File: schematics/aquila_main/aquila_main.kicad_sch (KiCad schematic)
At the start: 125 parts

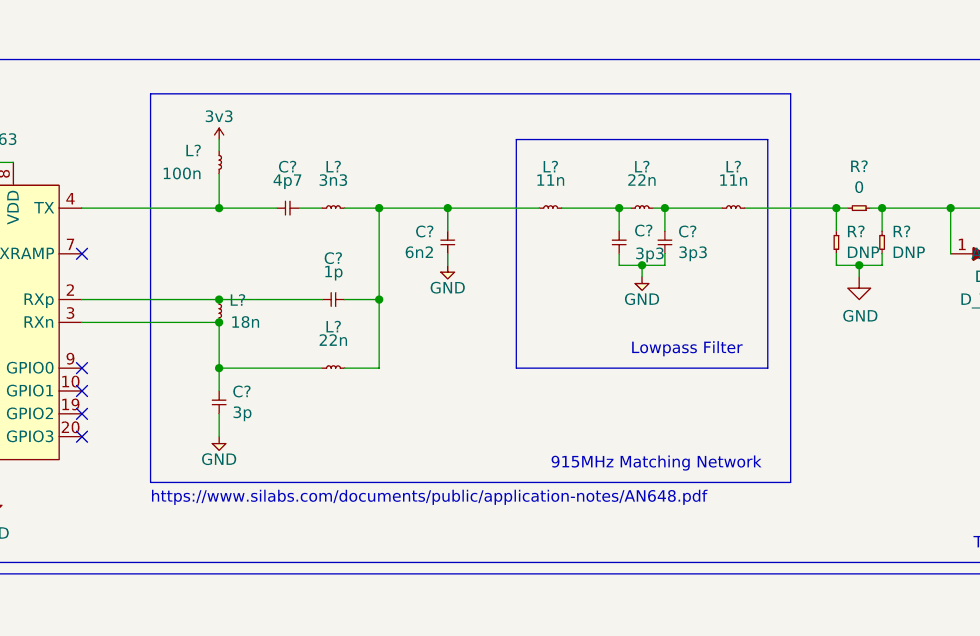
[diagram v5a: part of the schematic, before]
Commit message: changed to 868MHz matching on radio
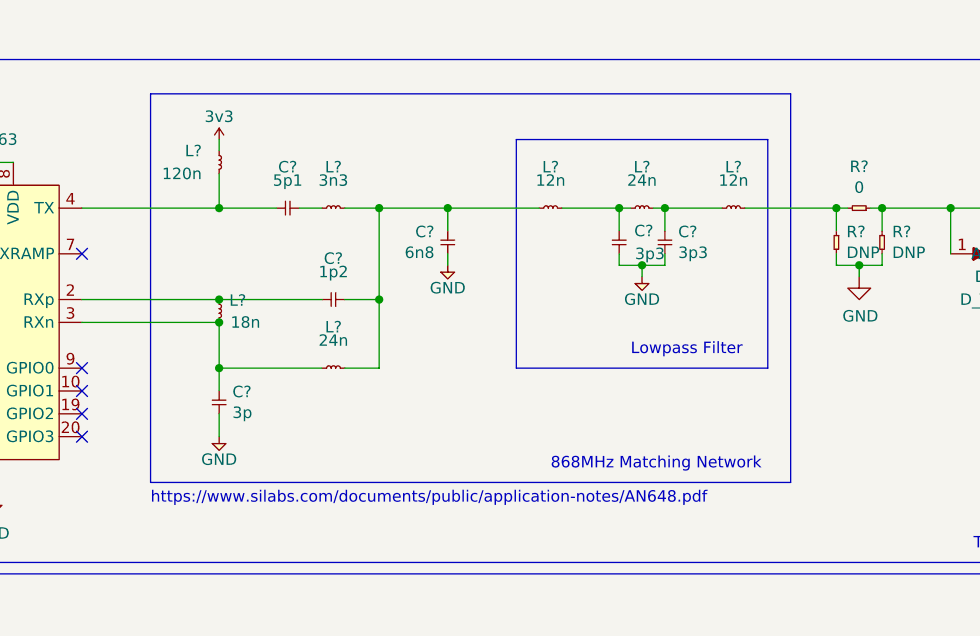
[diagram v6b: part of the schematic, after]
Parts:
- C?: value 1p -> 1p2
- C?: value 6n2 -> 6n8
- C?: value 4p7 -> 5p1
- L? (x2): value 11n -> 12n
- L?: value 100n -> 120n
- L? (x2): value 22n -> 24n
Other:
- note added: "868MHz Matching Network"
- note removed: "915MHz Matching Network"
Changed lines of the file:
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@@
     (effects (font (size 1.27 1.27)) (justify left bottom))
   )
-  (text "915MHz Matching Network" (at 148.59 191.77 0)
+  (text "868MHz Matching Network" (at 148.59 191.77 0)
     (effects (font (size 1.27 1.27)) (justify left bottom))
   )
@@
       (effects (font (size 1.27 1.27)) (justify bottom))
     )
-    (property "Value" "11n" (id 1) (at 148.59 158.75 0)
+    (property "Value" "12n" (id 1) (at 148.59 158.75 0)
       (effects (font (size 1.27 1.27)) (justify top))
     )
@@
       (effects (font (size 1.27 1.27)) (justify bottom))
     )
-    (property "Value" "1p" (id 1) (at 124.46 168.91 0)
+    (property "Value" "1p2" (id 1) (at 124.46 168.91 0)
       (effects (font (size 1.27 1.27)) (justify top))
     )
@@
       (effects (font (size 1.27 1.27)) (justify bottom))
     )
-    (property "Value" "11n" (id 1) (at 168.91 158.75 0)
+    (property "Value" "12n" (id 1) (at 168.91 158.75 0)
       (effects (font (size 1.27 1.27)) (justify top))
     )
@@
       (effects (font (size 1.27 1.27)) (justify left))
     )
-    (property "Value" "6n2" (id 1) (at 135.6868 167.513 90)
+    (property "Value" "6n8" (id 1) (at 135.6868 167.513 90)
       (effects (font (size 1.27 1.27)) (justify left))
     )
@@
       (effects (font (size 1.27 1.27)) (justify left))
     )
-    (property "Value" "100n" (id 1) (at 105.41 158.75 90)
+    (property "Value" "120n" (id 1) (at 105.41 158.75 90)
       (effects (font (size 1.27 1.27)) (justify left))
     )
@@
       (effects (font (size 1.27 1.27)) (justify bottom))
     )
-    (property "Value" "22n" (id 1) (at 124.46 176.53 0)
+    (property "Value" "24n" (id 1) (at 124.46 176.53 0)
       (effects (font (size 1.27 1.27)) (justify top))
     )
@@
       (effects (font (size 1.27 1.27)) (justify bottom))
     )
-    (property "Value" "22n" (id 1) (at 158.75 158.75 0)
+    (property "Value" "24n" (id 1) (at 158.75 158.75 0)
       (effects (font (size 1.27 1.27)) (justify top))
     )
@@
       (effects (font (size 1.27 1.27)) (justify bottom))
     )
-    (property "Value" "4p7" (id 1) (at 119.38 158.75 0)
+    (property "Value" "5p1" (id 1) (at 119.38 158.75 0)
       (effects (font (size 1.27 1.27)) (justify top))
     )
@@
     )
     (path "/2507031b-f5f8-4904-8f00-05c1469bcb72"
-      (reference "C?") (unit 1) (value "1p") (footprint "Strix:C_0402")
+      (reference "C?") (unit 1) (value "1p2") (footprint "Strix:C_0402")
     )
     (path "/27d5dca1-8f4b-4ac0-a3bf-f07d7733003c"
@@
     )
     (path "/689141ce-3cb4-4f7d-80d2-c503f350478d"
-      (reference "C?") (unit 1) (value "6n2") (footprint "Strix:C_0402")
+      (reference "C?") (unit 1) (value "6n8") (footprint "Strix:C_0402")
     )
     (path "/6e3a9897-4767-45ac-8e89-755b689b7b7b"
@@
     )
     (path "/b06b7fb7-53f6-4d89-b46b-9418e53b1ff3"
-      (reference "C?") (unit 1) (value "4p7") (footprint "Strix:C_0402")
+      (reference "C?") (unit 1) (value "5p1") (footprint "Strix:C_0402")
     )
     (path "/c80e54df-b29e-4bec-83f1-f7d3fca646ef"
@@
     )
     (path "/1288b0d7-80e7-4aa8-ba26-28318595760b"
-      (reference "L?") (unit 1) (value "11n") (footprint "Strix:L_0402")
+      (reference "L?") (unit 1) (value "12n") (footprint "Strix:L_0402")
     )
     (path "/2bcdfdc0-13c6-4c2e-9736-75366b3d43f9"
-      (reference "L?") (unit 1) (value "11n") (footprint "Strix:L_0402")
+      (reference "L?") (unit 1) (value "12n") (footprint "Strix:L_0402")
     )
     (path "/479753ae-6b30-4476-9bcb-23c9de27d17f"
@@
     )
     (path "/79bfbd2f-d120-4bb9-b75e-4a2b67982552"
-      (reference "L?") (unit 1) (value "100n") (footprint "Strix:L_0402")
+      (reference "L?") (unit 1) (value "120n") (footprint "Strix:L_0402")
     )
     (path "/7b0286f7-fbd0-424c-b380-5667a0d39bc5"
@@
     )
     (path "/89ed38eb-1140-4ef1-a212-5194d0297225"
-      (reference "L?") (unit 1) (value "22n") (footprint "Strix:L_0402")
+      (reference "L?") (unit 1) (value "24n") (footprint "Strix:L_0402")
     )
     (path "/af4782b6-37a5-400f-8446-daf53b8807d6"
-      (reference "L?") (unit 1) (value "22n") (footprint "Strix:L_0402")
+      (reference "L?") (unit 1) (value "24n") (footprint "Strix:L_0402")
     )
     (path "/de56e1d2-438f-4de1-963e-76768a4e6948"

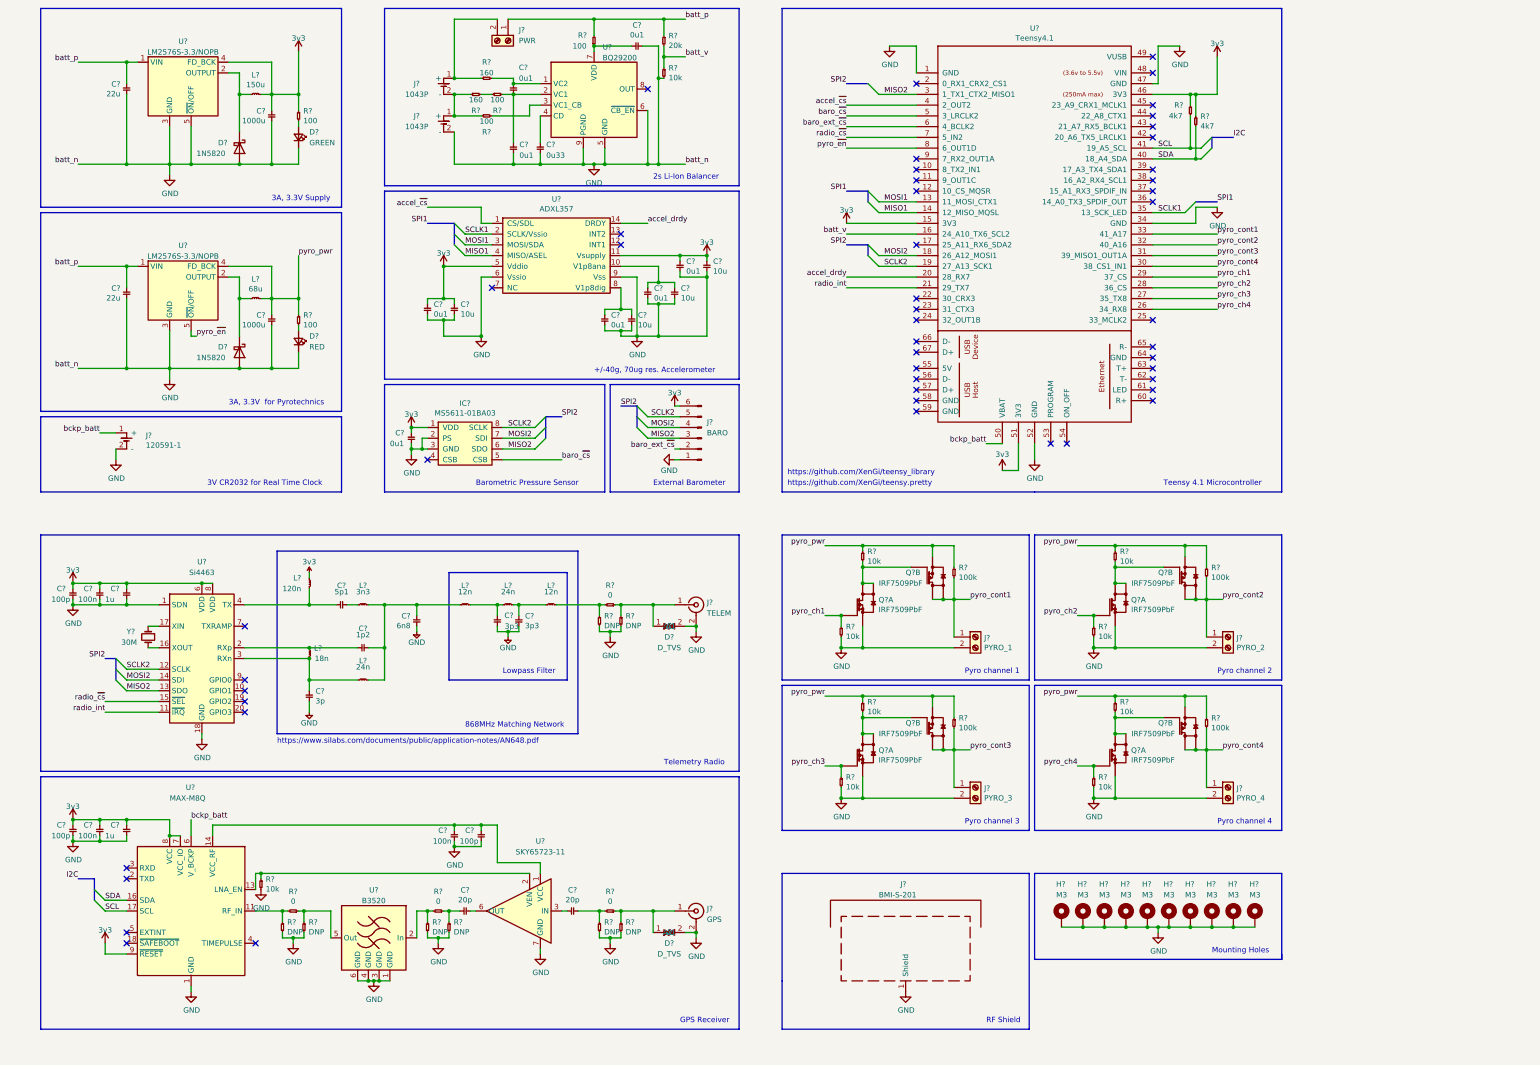
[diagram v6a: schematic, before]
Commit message: added pyro safety switch
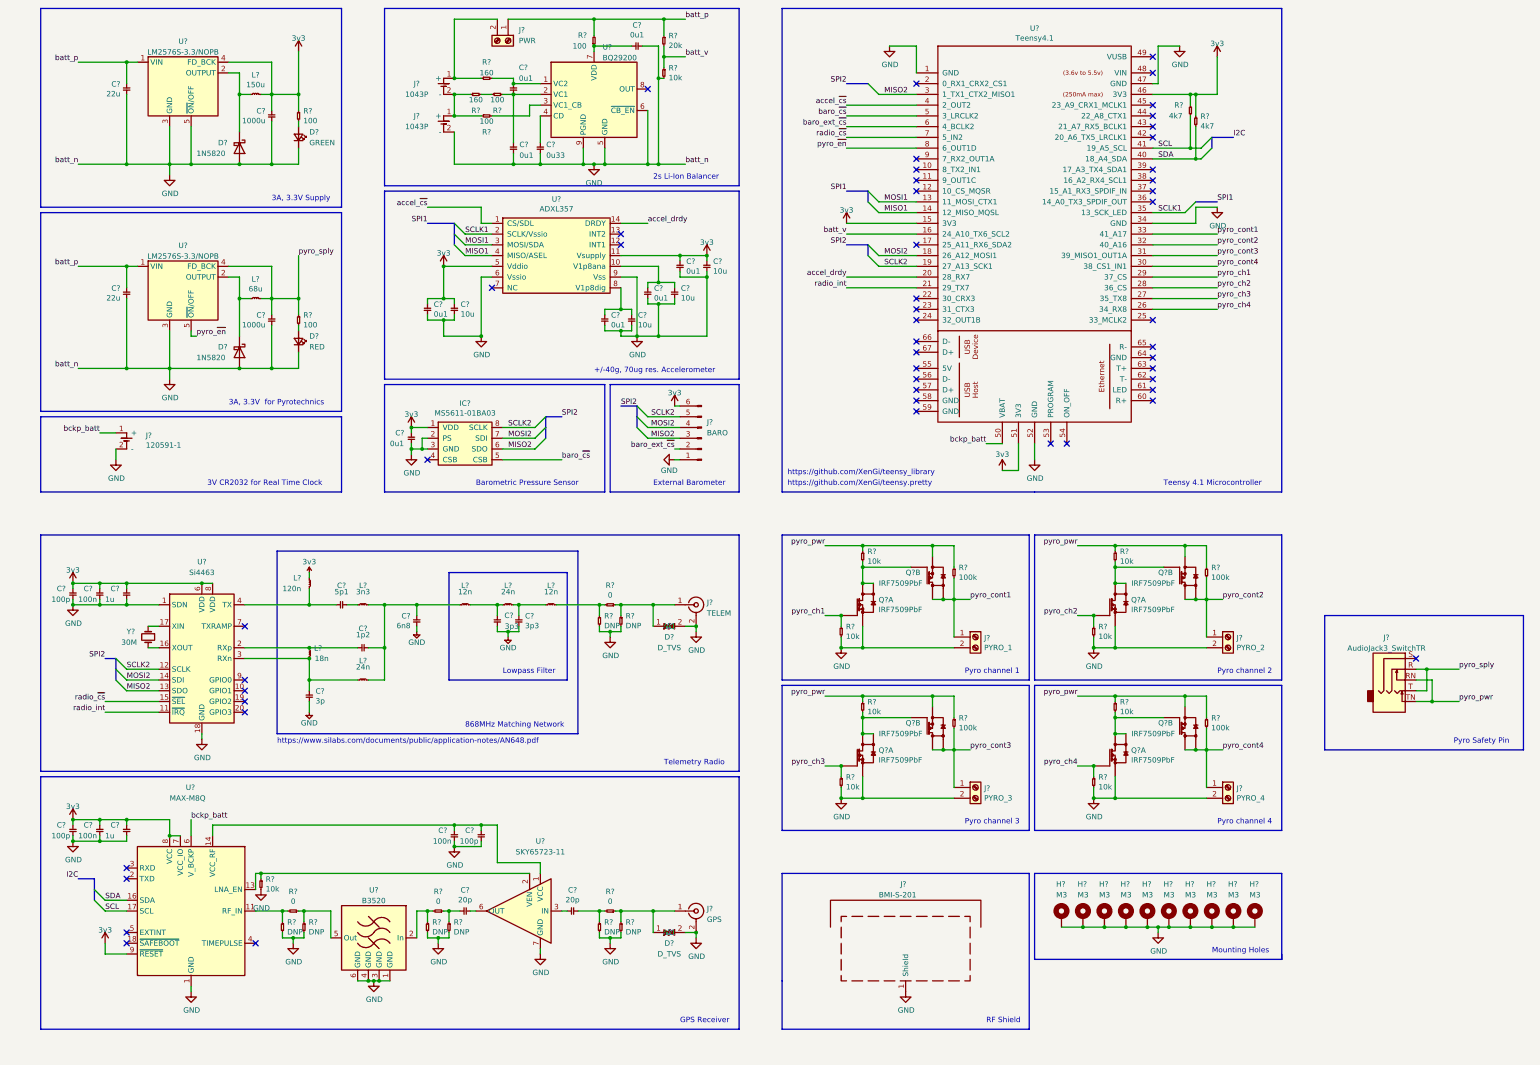
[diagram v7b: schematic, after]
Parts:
- added J?: AudioJack3_SwitchTR, aquila:audio_2.5mm_1501_02, symbol Connector:AudioJack3_SwitchTR
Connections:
- net pyro_pwr: now also J?.RN, J?.TN; no longer C?.1, L?.2, R?.1, U?.4 (FD_BCK)
- new net pyro_sply: C?.1, J?.R, J?.T, L?.2, R?.1, U?.4 (FD_BCK)
- no-connect marks 50 -> 51
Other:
- note added: "Pyro Safety Pin"
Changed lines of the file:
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@@
   (junction (at 111.76 172.72) (diameter 0) (color 0 0 0 0)
   )
+  (junction (at 377.19 185.42) (diameter 0) (color 0 0 0 0)
+  )
   (junction (at 323.85 161.29) (diameter 0) (color 0 0 0 0)
   )
@@
   (junction (at 158.75 168.91) (diameter 0) (color 0 0 0 0)
   )
+  (junction (at 375.92 177.8) (diameter 0) (color 0 0 0 0)
+  )
   (junction (at 102.87 106.68) (diameter 0) (color 0 0 0 0)
   )
@@
   (no_connect (at 255.27 62.23))
   (no_connect (at 255.27 64.77))
+  (no_connect (at 373.38 175.26))
   (no_connect (at 68.58 227.33))
   (no_connect (at 68.58 224.79))
@@
     (stroke (width 0) (type default) (color 0 0 0 0))
   )
+  (polyline (pts (xy 398.78 196.85) (xy 351.79 196.85))
+    (stroke (width 0) (type default) (color 0 0 0 0))
+  )
   (wire (pts (xy 302.26 149.86) (xy 302.26 148.59))
     (stroke (width 0) (type default) (color 0 0 0 0))
@@
     (stroke (width 0) (type default) (color 0 0 0 0))
   )
+  (wire (pts (xy 375.92 177.8) (xy 383.54 177.8))
+    (stroke (width 0) (type default) (color 0 0 0 0))
+  )
   (wire (pts (xy 78.74 58.42) (xy 78.74 60.96))
     (stroke (width 0) (type default) (color 0 0 0 0))
@@
     (stroke (width 0) (type default) (color 0 0 0 0))
   )
+  (polyline (pts (xy 398.78 165.1) (xy 398.78 196.85))
+    (stroke (width 0) (type default) (color 0 0 0 0))
+  )
   (wire (pts (xy 242.57 193.04) (xy 242.57 189.23))
     (stroke (width 0) (type default) (color 0 0 0 0))
@@
     (stroke (width 0) (type default) (color 0 0 0 0))
   )
+  (wire (pts (xy 373.38 180.34) (xy 377.19 180.34))
+    (stroke (width 0) (type default) (color 0 0 0 0))
+  )
   (wire (pts (xy 62.23 162.56) (xy 55.88 162.56))
     (stroke (width 0) (type default) (color 0 0 0 0))
@@
     (stroke (width 0) (type default) (color 0 0 0 0))
   )
+  (wire (pts (xy 375.92 182.88) (xy 373.38 182.88))
+    (stroke (width 0) (type default) (color 0 0 0 0))
+  )
   (polyline (pts (xy 281.94 180.34) (xy 281.94 146.05))
     (stroke (width 0) (type default) (color 0 0 0 0))
@@
     (stroke (width 0) (type default) (color 0 0 0 0))
   )
+  (polyline (pts (xy 351.79 165.1) (xy 398.78 165.1))
+    (stroke (width 0) (type default) (color 0 0 0 0))
+  )
   (wire (pts (xy 323.85 148.59) (xy 323.85 153.67))
     (stroke (width 0) (type default) (color 0 0 0 0))
@@
     (stroke (width 0) (type default) (color 0 0 0 0))
   )
+  (wire (pts (xy 377.19 180.34) (xy 377.19 185.42))
+    (stroke (width 0) (type default) (color 0 0 0 0))
+  )
   (wire (pts (xy 264.16 184.15) (xy 264.16 189.23))
     (stroke (width 0) (type default) (color 0 0 0 0))
@@
     (stroke (width 0) (type default) (color 0 0 0 0))
   )
+  (wire (pts (xy 373.38 177.8) (xy 375.92 177.8))
+    (stroke (width 0) (type default) (color 0 0 0 0))
+  )
+  (wire (pts (xy 377.19 185.42) (xy 373.38 185.42))
+    (stroke (width 0) (type default) (color 0 0 0 0))
+  )
   (polyline (pts (xy 341.63 146.05) (xy 283.21 146.05))
     (stroke (width 0) (type default) (color 0 0 0 0))
@@
     (stroke (width 0) (type default) (color 0 0 0 0))
   )
+  (wire (pts (xy 377.19 185.42) (xy 383.54 185.42))
+    (stroke (width 0) (type default) (color 0 0 0 0))
+  )
   (wire (pts (xy 259.08 184.15) (xy 264.16 184.15))
     (stroke (width 0) (type default) (color 0 0 0 0))
@@
     (stroke (width 0) (type default) (color 0 0 0 0))
   )
+  (polyline (pts (xy 351.79 196.85) (xy 351.79 165.1))
+    (stroke (width 0) (type default) (color 0 0 0 0))
+  )
   (wire (pts (xy 302.26 153.67) (xy 313.69 153.67))
     (stroke (width 0) (type default) (color 0 0 0 0))
@@
     (stroke (width 0) (type default) (color 0 0 0 0))
   )
+  (wire (pts (xy 375.92 177.8) (xy 375.92 182.88))
+    (stroke (width 0) (type default) (color 0 0 0 0))
+  )
   (bus (pts (xy 60.96 229.87) (xy 60.96 232.41))
     (stroke (width 0) (type default) (color 0 0 0 0))
@@
     (effects (font (size 1.27 1.27)) (justify left bottom))
   )
+  (text "Pyro Safety Pin" (at 382.27 195.58 0)
+    (effects (font (size 1.27 1.27)) (justify left bottom))
+  )
   (text "3A, 3.3V Supply" (at 102.87 67.31 0)
     (effects (font (size 1.27 1.27)) (justify left bottom))
@@
     (effects (font (size 1.27 1.27)) (justify right bottom))
   )
-  (label "pyro_pwr" (at 109.22 80.01 0)
+  (label "pyro_sply" (at 109.22 80.01 0)
     (effects (font (size 1.27 1.27)) (justify left bottom))
   )
@@
     (effects (font (size 1.27 1.27)) (justify right bottom))
   )
+  (label "pyro_pwr" (at 383.54 185.42 0)
+    (effects (font (size 1.27 1.27)) (justify left bottom))
+  )
   (label "pyro_ch2" (at 293.37 165.1 180)
     (effects (font (size 1.27 1.27)) (justify right bottom))
@@
     (effects (font (size 1.27 1.27)) (justify right bottom))
   )
+  (label "pyro_sply" (at 383.54 177.8 0)
+    (effects (font (size 1.27 1.27)) (justify left bottom))
+  )
   (label "MOSI1" (at 148.59 77.47 0)
     (effects (font (size 1.27 1.27)) (justify left bottom))
@@
     (pin "2")
   )
+  (symbol (lib_id "Connector:AudioJack3_SwitchTR") (at 368.3 177.8 0) (unit 1)
+    (in_bom yes) (on_board yes) (fields_autoplaced)
+    (property "Reference" "J?" (id 0) (at 366.395 170.2902 0))
+    (property "Value" "AudioJack3_SwitchTR" (id 1) (at 366.395 172.8271 0))
+    (property "Footprint" "aquila:audio_2.5mm_1501_02" (id 2) (at 368.3 177.8 0)
+      (effects (font (size 1.27 1.27)) hide)
+    )
+    (property "Datasheet" "https://www.farnell.com/datasheets/1918696.pdf" (id 3) (at 368.3 177.8 0)
+      (effects (font (size 1.27 1.27)) hide)
+    )
+    (property "farnell" "1216976" (id 4) (at 368.3 177.8 0)
+      (effects (font (size 1.27 1.27)) hide)
+    )
+    (pin "R")
+    (pin "RN")
+    (pin "S")
+    (pin "T")
+    (pin "TN")
+  )
   (symbol (lib_id "aquila:R-cusf-kicad") (at 264.16 189.23 270) (unit 1)
     (in_bom yes) (on_board yes)
@@
       (reference "J?") (unit 1) (value "PWR") (footprint "")
     )
+    (path "/99c1f101-5d22-400f-9743-bb2f2b4a649e"
+      (reference "J?") (unit 1) (value "AudioJack3_SwitchTR") (footprint "aquila:audio_2.5mm_1501_02")
+    )
     (path "/d2a2af03-5cef-466b-b6f2-22346d252541"
